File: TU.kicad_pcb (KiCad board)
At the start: 4 copper layers, 48.3 x 109.2 mm, 134 parts, among them IC1 CC1190, J1 Conn_01x06_Male, J2 Conn_01x17_Male, J3 Conn_01x05_Male, J4 Debugger connector, J5 ARM_JTAG_SWD_10, J6 Conn_01x05_Male, U1 ADP150AUJZ-3.3-R7, U2 SN65HVD233, U3 CC1200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

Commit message: Added PA shield
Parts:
- removed G***: LOGO, KTHFS:simon_richter
- added J7: RF_Shield_One_Piece, TU-HW RF LIB:WE_shield_20x20_36503205S, F.Cu at (97.5, 59.2)
- moved C13 3.60 mm to (116.4, 64.2), turned to 270 degrees
- moved J6 1.84 mm to (90.9, 35.4)
- moved L3 1.71 mm to (114.8, 64.2)
- moved J3 1.46 mm to (101.8, 35.4)
- moved C11 1.38 mm to (117.9, 64.3)
- moved C7 1.05 mm to (100.2, 44.1), turned to 270 degrees
- moved C74 0.75 mm to (115.7, 68.3), turned to 0 degrees
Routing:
- net Net-(IC1-Pad10): track 0.00 -> 11.0 mm
- net +3V3: track 87.4 -> 88.7 mm
- net Net-(IC1-Pad6): track 14.6 -> 15.1 mm
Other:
- board text added: "Backup"
- board text added: "Main"
- board text removed: "Backup RF"
- board text removed: "Main RF"

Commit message: preliminairy routing of 50 ohm traces
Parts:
- moved C75 0.87 mm to (112.4, 68.5)
- moved L17 0.87 mm to (112.4, 67.0)
- moved R7 0.68 mm to (108.2, 64.4)
- moved L14 0.30 mm to (113.2, 70.8)
- moved C74 0.24 mm to (115.7, 68.5)
- moved C17 0.23 mm to (101.7, 67.0)
- moved FL1 0.21 mm to (107.6, 67.0)
- moved L5 0.20 mm to (104.0, 66.2)
- moved C14 0.11 mm to (110.4, 55.4)
- moved C38 0.11 mm to (107.1, 47.9)
- moved R4 0.09 mm to (108.2, 56.1)
- moved C8 0.09 mm to (105.6, 43.4)
- moved C71 0.09 mm to (113.2, 73.9)
- moved L13 0.09 mm to (111.7, 73.9)
- moved C12 0.08 mm to (107.4, 59.9)
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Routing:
- net GND: track 60.5 -> 77.0 mm, vias 71 -> 95
- net Net-(C72-Pad1): track 0.00 -> 10.4 mm
- net /CC1190/ANTENNA_OUT: track 0.02 -> 9.55 mm
- net Net-(J2-Pad1): track 0.00 -> 8.34 mm
- net /CC1190/RFIO: track 0.00 -> 7.99 mm
- net /CAN_transceiver/CAN_RX_1: track 0.00 -> 7.50 mm
- net /transceiver/VDD_CC1200: track 60.5 -> 68.0 mm
- net Net-(C17-Pad1): track 0.00 -> 7.03 mm
- net /CAN_transceiver/CAN_RX_2: track 0.00 -> 6.11 mm
- net Net-(C71-Pad1): track 0.00 -> 6.09 mm
- net Net-(C10-Pad1): track 0.00 -> 6.06 mm
- net Net-(C73-Pad2): track 0.00 -> 5.98 mm
- net /CAN_transceiver/CAN_TX_2: track 0.85 -> 6.44 mm
- net Net-(C76-Pad2): track 0.00 -> 5.52 mm
- net Net-(C73-Pad1): track 0.00 -> 5.48 mm
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
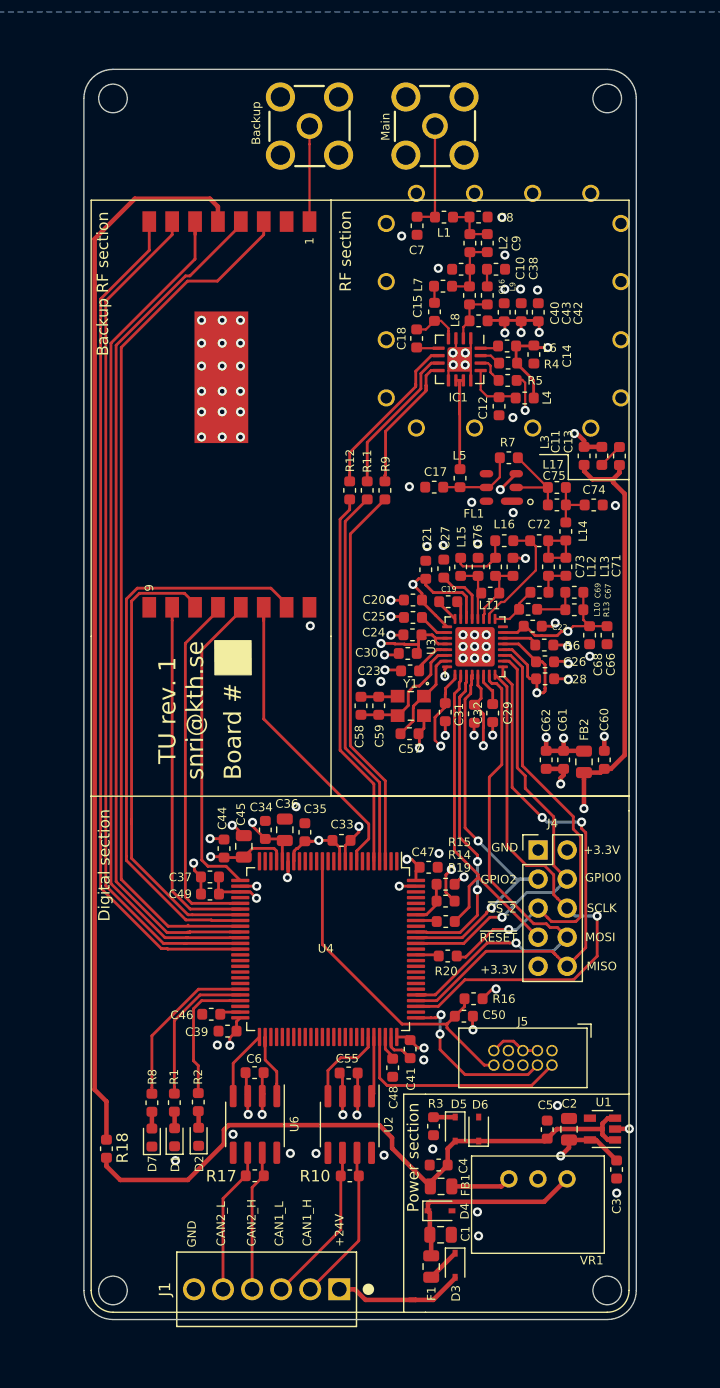
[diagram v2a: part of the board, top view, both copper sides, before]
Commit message: Added guard ring and cleaned up silkscreen
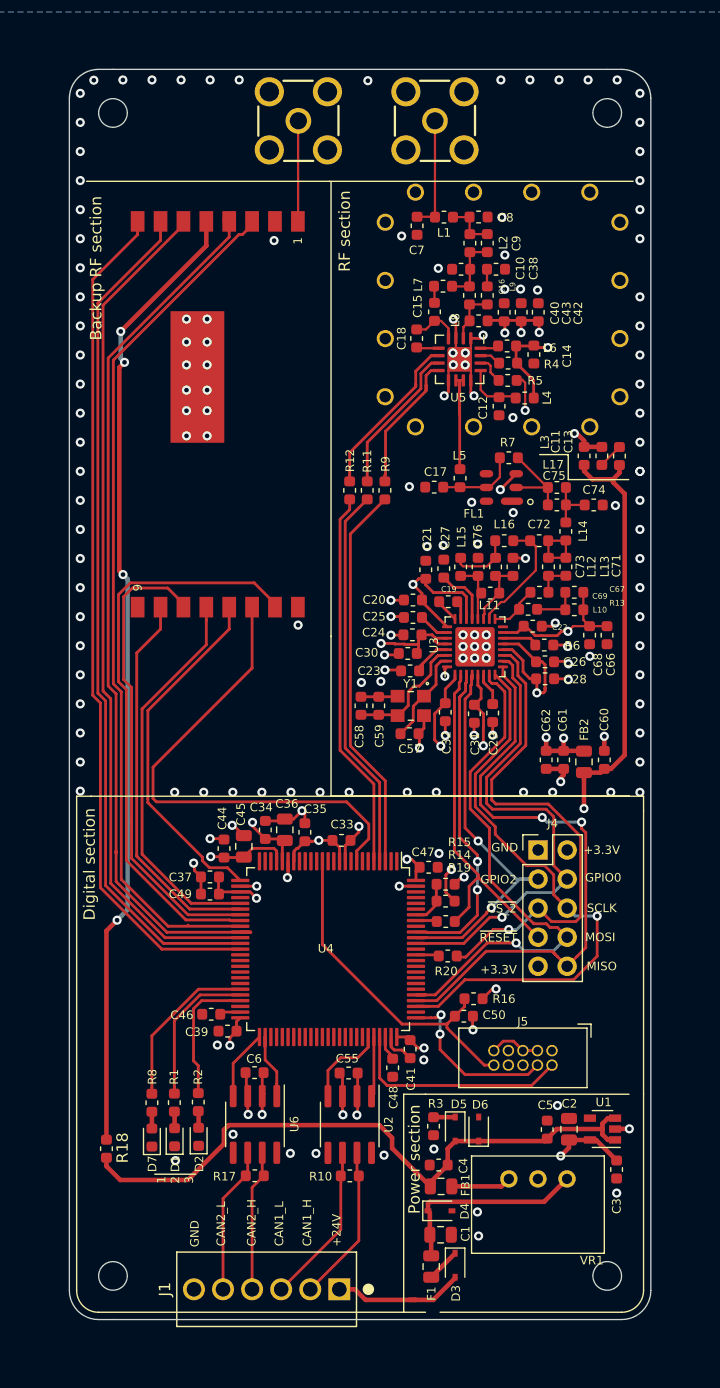
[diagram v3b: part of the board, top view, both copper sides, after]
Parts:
- L4: value L -> 1.5n
- moved J7 18.2 mm to (100.1, 41.2), turned to 0 degrees
- moved H3 1.27 mm to (73.7, 135.9)
- moved H4 1.27 mm to (116.8, 135.9)
- moved H1 1.27 mm to (73.7, 34.3)
- moved H2 1.27 mm to (116.8, 34.3)
- moved J6 1.07 mm to (89.9, 35.0)
- moved J2 1.02 mm to (72.8, 51.0)
- moved J3 0.46 mm to (101.8, 35.0)
- renumbered IC1 to U5
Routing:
- net /RESET_RF2: track 27.6 -> 43.8 mm
- net GND: track 77.0 -> 88.3 mm, vias 95 -> 168
- net Net-(J2-Pad5): track 92.9 -> 84.7 mm, vias 0 -> 4
- net /GPIO0: track 37.2 -> 42.4 mm
- net /~CS_1: track 39.2 -> 44.4 mm
- net /MISO: track 47.3 -> 52.3 mm
- net /~CS_RF2: track 27.6 -> 31.1 mm
- net /SCLK_RF2: track 31.5 -> 34.3 mm
- net /SCLK: track 49.1 -> 51.6 mm
- net /DIO4: track 75.3 -> 77.3 mm
- net /MISO_RF2: track 31.7 -> 33.7 mm
- net /MOSI: track 44.6 -> 46.2 mm
- net /DIO3: track 76.5 -> 75.1 mm
- net /DIO0: track 75.4 -> 74.3 mm
- net /DIO5: track 50.2 -> 50.9 mm
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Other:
- board size 48.3 x 109.2 mm -> 50.8 x 109.2 mm
- board text added: "1 2 3"
- board text removed: "Backup"
- board text removed: "Board #"
- board text removed: "Main"
- board text removed: "TU rev. 1 snri@kth.se"

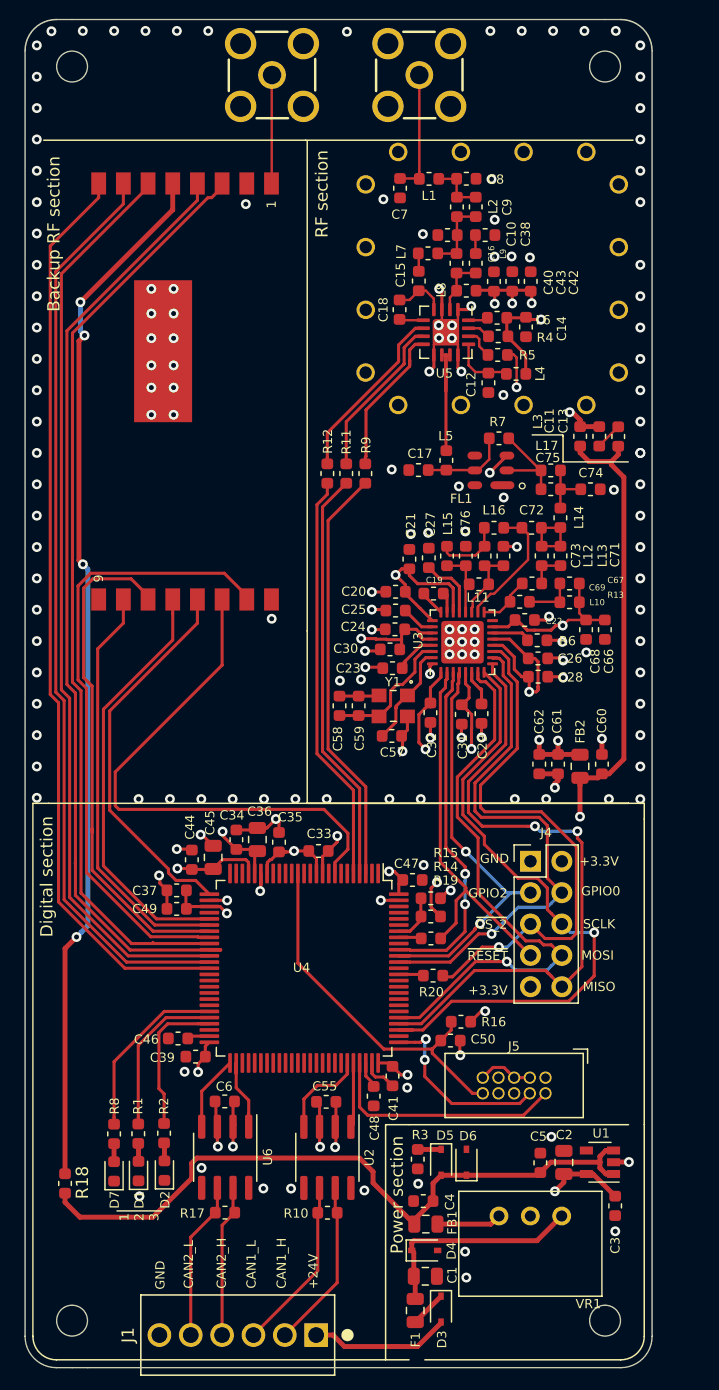
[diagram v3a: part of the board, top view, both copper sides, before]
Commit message: Changed track width for 50 ohm traces
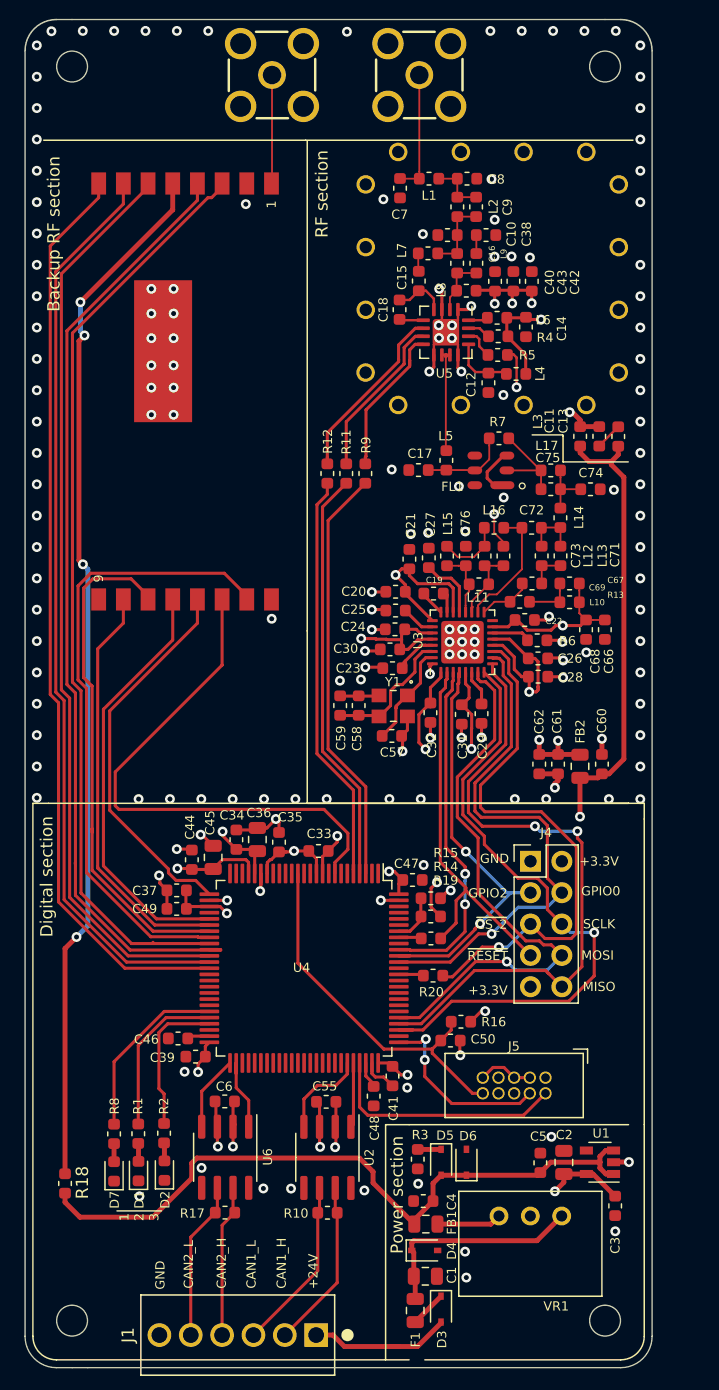
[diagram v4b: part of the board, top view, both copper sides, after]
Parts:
- moved C58 1.55 mm to (96.9, 86.1)
- moved C59 1.50 mm to (95.4, 86.1)
- moved C42 0.09 mm to (110.9, 51.7)
- moved C43 0.09 mm to (109.4, 51.7)
- moved C40 0.09 mm to (107.9, 51.7)
- moved C38 0.07 mm to (107.2, 47.9)
- moved C8 0.06 mm to (105.7, 43.4)
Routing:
- net GND: track 88.3 -> 92.4 mm, vias 168 -> 166
- net Net-(L5-Pad2): track 11.0 -> 8.42 mm
- net /transceiver/VDD_CC1200: track 68.3 -> 69.9 mm
- net Net-(C71-Pad1): track 6.09 -> 4.64 mm
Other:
- rule trace_min: 0.2 -> 0.15

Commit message: Small changes to routing
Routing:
- net GND: track 92.4 -> 128.2 mm
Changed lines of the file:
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@@
     (thickness 1.6)
     (drawings 67)
-    (tracks 1086)
+    (tracks 1102)
     (zones 0)
     (modules 134)
@@
   (segment (start 98.47742 85.2931) (end 98.52976 85.24076) (width 0.25) (layer F.Cu) (net 1) (status 30))
   (segment (start 95.3262 85.2931) (end 98.47742 85.2931) (width 0.25) (layer F.Cu) (net 1) (status 30))
-  (via (at 100.4316 89.7636) (size 0.8) (drill 0.4) (layers F.Cu B.Cu) (net 1))
   (segment (start 100.4316 88.5951) (end 100.3555 88.519) (width 0.25) (layer F.Cu) (net 1) (status 30))
-  (segment (start 100.4316 89.7636) (end 100.4316 88.5951) (width 0.25) (layer F.Cu) (net 1) (status 20))
   (segment (start 99.0001 78.2828) (end 99.0809 78.3636) (width 0.25) (layer F.Cu) (net 1) (status 30))
   (segment (start 97.9424 78.2828) (end 99.0001 78.2828) (width 0.25) (layer F.Cu) (net 1) (status 20))
@@
   (segment (start 98.75002 82.95132) (end 98.8313 83.0326) (width 0.25) (layer F.Cu) (net 1) (status 30))
   (segment (start 97.41916 82.95132) (end 98.75002 82.95132) (width 0.25) (layer F.Cu) (net 1) (status 20))
-  (via (at 95.36176 84.04352) (size 0.8) (drill 0.4) (layers F.Cu B.Cu) (net 1))
-  (via (at 97.06356 83.947) (size 0.8) (drill 0.4) (layers F.Cu B.Cu) (net 1))
   (via (at 117.6655 128.651) (size 0.8) (drill 0.4) (layers F.Cu B.Cu) (net 1))
   (segment (start 109.67199 57.86333) (end 109.67199 60.27407) (width 0.2) (layer F.Cu) (net 1))
@@
   (segment (start 108.613 65.80774) (end 107.288 67.13274) (width 0.25) (layer F.Cu) (net 1))
   (segment (start 108.888 65.80774) (end 108.613 65.80774) (width 0.25) (layer F.Cu) (net 1))
+  (segment (start 100.4316 89.7636) (end 100.4316 88.5951) (width 0.25) (layer F.Cu) (net 1) (status 20))
+  (via (at 100.4316 89.7636) (size 0.8) (drill 0.4) (layers F.Cu B.Cu) (net 1))
+  (via (at 95.36176 84.04352) (size 0.8) (drill 0.4) (layers F.Cu B.Cu) (net 1))
+  (via (at 97.06356 83.947) (size 0.8) (drill 0.4) (layers F.Cu B.Cu) (net 1))
+  (segment (start 87.31758 32.4358) (end 87.31758 31.99346) (width 0.25) (layer F.Cu) (net 1))
+  (segment (start 86.27868 31.03456) (end 102.50868 31.03456) (width 0.25) (layer F.Cu) (net 1))
+  (segment (start 102.50868 31.03456) (end 106.01868 31.03456) (width 0.25) (layer F.Cu) (net 1))
+  (segment (start 99.2505 32.4358) (end 99.2505 32.01638) (width 0.4) (layer F.Cu) (net 1))
+  (segment (start 99.2505 32.01638) (end 98.44868 31.21456) (width 0.4) (layer F.Cu) (net 1))
+  (segment (start 98.44868 31.21456) (end 100.39868 31.21456) (width 0.4) (layer F.Cu) (net 1))
+  (segment (start 100.39868 31.21456) (end 105.51868 31.21456) (width 0.4) (layer F.Cu) (net 1))
+  (segment (start 92.39758 32.4358) (end 92.39758 31.99566) (width 0.4) (layer F.Cu) (net 1))
+  (segment (start 92.39758 31.99566) (end 93.20868 31.18456) (width 0.4) (layer F.Cu) (net 1))
+  (segment (start 93.20868 31.18456) (end 91.08868 31.18456) (width 0.4) (layer F.Cu) (net 1))
+  (segment (start 87.31758 32.4358) (end 87.31758 31.96566) (width 0.4) (layer F.Cu) (net 1))
+  (segment (start 87.31758 31.96566) (end 88.06868 31.21456) (width 0.4) (layer F.Cu) (net 1))
+  (segment (start 87.31758 32.07346) (end 86.27868 31.03456) (width 0.25) (layer F.Cu) (net 1))
+  (segment (start 87.31758 32.4358) (end 87.31758 32.07346) (width 0.25) (layer F.Cu) (net 1))
   (segment (start 101.45996 132.41162) (end 101.34288 132.29454) (width 0.4) (layer F.Cu) (net 2) (status 30))
   (segment (start 101.45996 134.1335) (end 101.45996 132.41162) (width 0.4) (layer F.Cu) (net 2) (status 30))
@@
   (segment (start 100.6559 79.8876) (end 100.9473 80.179) (width 0.25) (layer F.Cu) (net 16) (status 30))
   (segment (start 105.53876 85.72324) (end 105.3592 85.9028) (width 0.25) (layer F.Cu) (net 16) (status 30))
-  (segment (start 105.820812 85.441188) (end 105.820812 84.586412) (width 0.25) (layer F.Cu) (net 16))
-  (segment (start 105.3592 85.9028) (end 105.820812 85.441188) (width 0.25) (layer F.Cu) (net 16) (status 10))
   (via (at 106.0196 89.5731) (size 0.8) (drill 0.4) (layers F.Cu B.Cu) (net 16))
-  (segment (start 105.53876 84.30436) (end 105.53876 83.3665) (width 0.25) (layer F.Cu) (net 16) (status 20))
-  (segment (start 105.820812 84.586412) (end 105.53876 84.30436) (width 0.25) (layer F.Cu) (net 16))
   (segment (start 102.85126 80.179) (end 101.83489 80.179) (width 0.25) (layer F.Cu) (net 16) (status 10))
   (segment (start 100.3554 80.1371) (end 100.6095 79.883) (width 0.25) (layer F.Cu) (net 16) (status 30))
@@
   (segment (start 114.8462 79.5782) (end 115.2989 79.1255) (width 0.25) (layer F.Cu) (net 16))
   (segment (start 113.411 79.5782) (end 114.8462 79.5782) (width 0.25) (layer F.Cu) (net 16))
+  (segment (start 105.53876 83.904) (end 105.53876 83.3665) (width 0.25) (layer F.Cu) (net 16))
+  (segment (start 105.53876 85.14754) (end 105.53876 83.904) (width 0.25) (layer F.Cu) (net 16))
+  (segment (start 105.2322 85.4541) (end 105.53876 85.14754) (width 0.25) (layer F.Cu) (net 16))
+  (segment (start 105.2322 85.9916) (end 105.2322 85.4541) (width 0.25) (layer F.Cu) (net 16))
   (segment (start 102.31376 81.179) (end 102.85126 81.179) (width 0.25) (layer F.Cu) (net 17) (status 20))
   (segment (start 102.092918 81.179) (end 102.31376 81.179) (width 0.25) (layer F.Cu) (net 17))
@@
   (segment (start 102.56012 74.88438) (end 103.41312 75.73738) (width 0.25) (layer F.Cu) (net 19) (status 10))
   (segment (start 103.41312 75.73738) (end 104.364085 75.737381) (width 0.25) (layer F.Cu) (net 19))
-  (segment (start 106.03876 84.04041) (end 106.03876 83.3665) (width 0.25) (layer F.Cu) (net 20) (status 20))
-  (segment (start 106.726548 84.728198) (end 106.03876 84.04041) (width 0.25) (layer F.Cu) (net 20))
-  (segment (start 106.8324 84.728198) (end 106.726548 84.728198) (width 0.25) (layer F.Cu) (net 20))
-  (segment (start 106.8324 85.9281) (end 106.8324 84.728198) (width 0.25) (layer F.Cu) (net 20) (status 10))
+  (segment (start 106.8324 84.83405) (end 106.8324 85.9281) (width 0.25) (layer F.Cu) (net 20))
+  (segment (start 106.03876 83.3665) (end 106.03876 84.04041) (width 0.25) (layer F.Cu) (net 20))
+  (segment (start 106.03876 84.04041) (end 106.8324 84.83405) (width 0.25) (layer F.Cu) (net 20))
   (segment (start 106.4125 47.94382) (end 106.41118 47.9425) (width 0.15) (layer F.Cu) (net 21))
   (segment (start 106.4125 49.441) (end 106.4125 47.94382) (width 0.15) (layer F.Cu) (net 21))
@@
   (segment (start 94.33814 68.94699) (end 93.49998 69.78515) (width 0.25) (layer F.Cu) (net 42))
   (segment (start 94.33814 68.04924) (end 94.33814 68.94699) (width 0.25) (layer F.Cu) (net 42) (status 10))
-  (segment (start 93.49998 69.78515) (end 93.499981 89.958191) (width 0.25) (layer F.Cu) (net 42))
   (segment (start 93.499981 89.958191) (end 96.456 92.91421) (width 0.25) (layer F.Cu) (net 42))
+  (segment (start 93.49998 69.78515) (end 93.499981 89.958191) (width 0.25) (layer F.Cu) (net 42))
   (segment (start 96.956 92.7778) (end 96.956 99.6654) (width 0.25) (layer F.Cu) (net 43) (status 20))
   (segment (start 96.956 92.7778) (end 93.94999 89.77179) (width 0.25) (layer F.Cu) (net 43))
@@
   (segment (start 103.941039 57.789239) (end 103.95 57.7982) (width 0.25) (layer F.Cu) (net 86))
   (segment (start 103.941039 57.653761) (end 103.941039 57.789239) (width 0.25) (layer F.Cu) (net 86))
-  (segment (start 103.941039 57.789239) (end 103.941039 65.40808) (width 0.15) (layer F.Cu) (net 86))
+  (segment (start 103.941039 57.653761) (end 103.941039 58.032201) (width 0.4) (layer F.Cu) (net 86))
+  (segment (start 103.941039 57.789239) (end 103.941039 58.032201) (width 0.15) (layer F.Cu) (net 86))
+  (segment (start 103.941039 58.032201) (end 103.941039 58.122201) (width 0.4) (layer F.Cu) (net 86))
+  (segment (start 103.941039 58.122201) (end 103.941039 65.40808) (width 0.15) (layer F.Cu) (net 86))
   (segment (start 107.106699 54.841261) (end 107.30288 54.64508) (width 0.2) (layer F.Cu) (net 87) (status 30))
   (segment (start 105.782839 54.841261) (end 107.106699 54.841261) (width 0.2) (layer F.Cu) (net 87) (status 30))

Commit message: Added ncab logo
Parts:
- added G***: LOGO, KTHFS:NCAB, F.Cu at (81.6, 86.0)
